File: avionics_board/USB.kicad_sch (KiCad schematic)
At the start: 3 parts, among them J11 10155435-00011LF

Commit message: checking AUX and SCI, tweak BOM
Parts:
- J11: MANUFACTURER (none) -> Amphenol; Manufacturer Amphenol -> (none); PARTREV (none) -> 10155435-00011LF; Part Number 10155435-00011LF -> (none)
- R43, R44: MANUFACTURER (none) -> YAGEO; Manufacturer YAGEO -> (none); PARTREV (none) -> RC0402FR-075K1L; Part Number RC0402FR-075K1L -> (none)
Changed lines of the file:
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@@
-			)
-		)
-		(property "Manufacturer" "YAGEO"
-			(at 175.895 94.615 0)
-			(effects
-				(font
-					(size 1.27 1.27)
-				)
-				(hide yes)
-			)
-		)
-		(property "Part Number" "RC0402FR-075K1L"
-			(at 175.895 94.615 0)
-			(effects
-				(font
-					(size 1.27 1.27)
-				)
-				(hide yes)
 			)
 		)
@@
 			)
 		)
-		(property "MANUFACTURER" ""
+		(property "MANUFACTURER" "YAGEO"
 			(at 175.895 94.615 0)
 			(effects
@@
 			)
 		)
-		(property "PARTREV" ""
+		(property "PARTREV" "RC0402FR-075K1L"
 			(at 175.895 94.615 0)
 			(effects
@@
 			(project "sci_board"
 				(path "/b4b2c88d-f6cd-4e60-862d-e21f68728580/840799ac-4fe6-4a8e-96a2-299affeec8e4/6b5440ce-79ea-4c41-89e9-7a3077535944"
-					(reference "R16")
+					(reference "R18")
 					(unit 1)
 				)
@@
 			)
 		)
-		(property "Manufacturer" "YAGEO"
-			(at 132.08 81.915 0)
-			(effects
-				(font
-					(size 1.27 1.27)
-				)
-				(hide yes)
-			)
-		)
-		(property "Part Number" "RC0402FR-075K1L"
-			(at 132.08 81.915 0)
-			(effects
-				(font
-					(size 1.27 1.27)
-				)
-				(hide yes)
-			)
-		)
 		(property "Tolerance" "1"
 			(at 132.08 81.915 0)
@@
 			)
 		)
-		(property "MANUFACTURER" ""
+		(property "MANUFACTURER" "YAGEO"
 			(at 132.08 81.915 0)
 			(effects
@@
 			)
 		)
-		(property "PARTREV" ""
+		(property "PARTREV" "RC0402FR-075K1L"
 			(at 132.08 81.915 0)
 			(effects
@@
 			(project "sci_board"
 				(path "/b4b2c88d-f6cd-4e60-862d-e21f68728580/840799ac-4fe6-4a8e-96a2-299affeec8e4/6b5440ce-79ea-4c41-89e9-7a3077535944"
-					(reference "R15")
+					(reference "R17")
 					(unit 1)
 				)
@@
 			)
 		)
-		(property "Description" ""
+		(property "Description" "USB connector"
 			(at 153.67 89.535 0)
 			(effects
@@
 			)
 		)
-		(property "Manufacturer" "Amphenol"
-			(at 153.67 89.535 0)
-			(effects
-				(font
-					(size 1.27 1.27)
-				)
-				(hide yes)
-			)
-		)
-		(property "Part Number" " 10155435-00011LF"
-			(at 153.67 89.535 0)
-			(effects
-				(font
-					(size 1.27 1.27)
-				)
-				(hide yes)
-			)
-		)
-		(property "MANUFACTURER" ""
+		(property "MANUFACTURER" "Amphenol"
 			(at 153.67 89.535 0)
 			(effects
@@
 			)
 		)
-		(property "PARTREV" ""
-			(at 153.67 89.535 0)
-			(effects
+		(property "PARTREV" " 10155435-00011LF"
+			(at 153.67 89.535 0)
+			(effects

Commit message: check BOM and footprints for SCI and AUX
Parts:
- R43, R44: Note (none) -> USB
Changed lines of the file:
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@@
+			)
+		)
+		(property "Note" "USB"
+			(at 175.895 94.615 0)
+			(effects
+				(font
+					(size 1.27 1.27)
+				)
+				(hide yes)
 			)
 		)
@@
 			(at 132.08 81.915 0)
 			(effects
+				(font
+					(size 1.27 1.27)
+				)
+				(hide yes)
+			)
+		)
+		(property "Note" "USB"
+			(at 132.08 81.915 0)
+			(effects

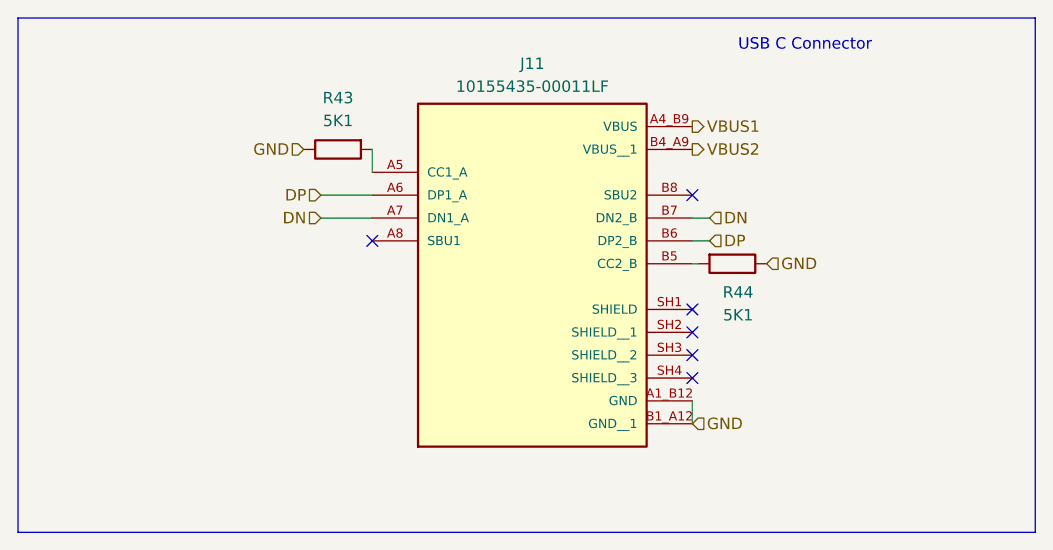
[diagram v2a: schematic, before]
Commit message: full science board with camera switches
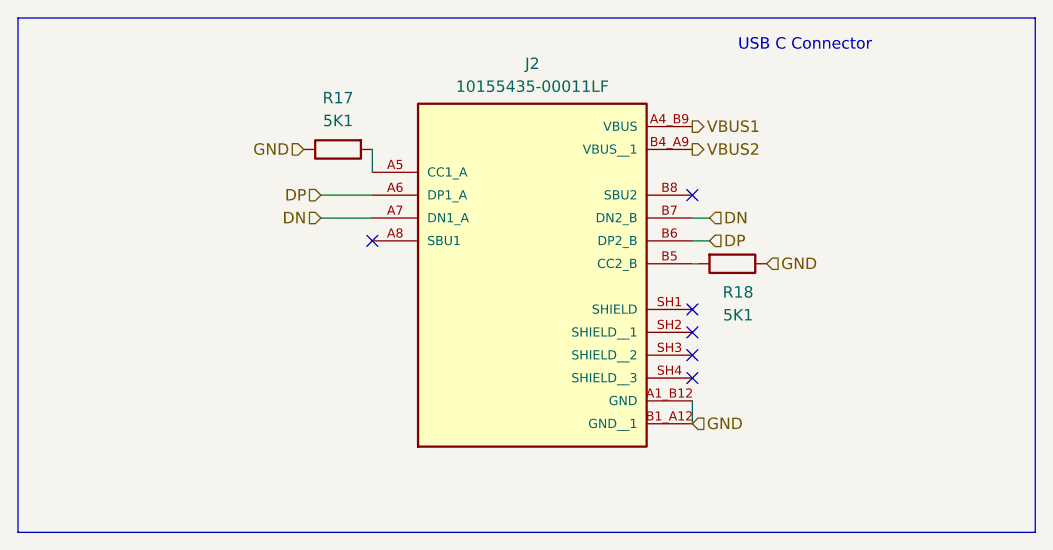
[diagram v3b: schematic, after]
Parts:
- renumbered J11 to J2, R43 to R17, R44 to R18
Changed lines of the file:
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@@
 (kicad_sch
-	(version 20231120)
+	(version 20250114)
 	(generator "eeschema")
-	(generator_version "8.0")
+	(generator_version "9.0")
 	(paper "A4")
-	(no_connect
-		(at 171.45 86.995)
-	)
-	(no_connect
-		(at 171.45 102.235)
-	)
-	(no_connect
-		(at 171.45 107.315)
-	)
-	(no_connect
-		(at 171.45 99.695)
-	)
-	(no_connect
-		(at 135.89 92.075)
-	)
-	(no_connect
-		(at 171.45 104.775)
-	)
-	(wire
-		(pts
-			(xy 173.355 92.075) (xy 171.45 92.075)
-		)
-		(stroke
-			(width 0)
-			(type default)
-		)
-	)
-	(wire
-		(pts
-			(xy 173.355 89.535) (xy 171.45 89.535)
-		)
-		(stroke
-			(width 0)
-			(type default)
-		)
-	)
-	(wire
-		(pts
-			(xy 130.175 89.535) (xy 135.89 89.535)
-		)
-		(stroke
-			(width 0)
-			(type default)
-		)
-	)
-	(wire
-		(pts
-			(xy 130.175 86.995) (xy 135.89 86.995)
-		)
-		(stroke
-			(width 0)
-			(type default)
-		)
-	)
-	(wire
-		(pts
-			(xy 135.89 81.915) (xy 135.89 84.455)
-		)
-		(stroke
-			(width 0)
-			(type default)
-		)
-	)
-	(wire
-		(pts
-			(xy 171.45 109.855) (xy 171.45 112.395)
-		)
-		(stroke
-			(width 0)
-			(type default)
-		)
-	)
-	(wire
-		(pts
-			(xy 172.085 94.615) (xy 171.45 94.615)
-		)
-		(stroke
-			(width 0)
-			(type default)
-		)
-	)
 	(rectangle
 		(start 96.52 67.31)
@@
 		)
 	)
+	(no_connect
+		(at 171.45 86.995)
+	)
+	(no_connect
+		(at 171.45 102.235)
+	)
+	(no_connect
+		(at 171.45 107.315)
+	)
+	(no_connect
+		(at 171.45 99.695)
+	)
+	(no_connect
+		(at 135.89 92.075)
+	)
+	(no_connect
+		(at 171.45 104.775)
+	)
+	(wire
+		(pts
+			(xy 173.355 92.075) (xy 171.45 92.075)
+		)
+		(stroke
+			(width 0)
+			(type default)
+		)
+	)
+	(wire
+		(pts
+			(xy 173.355 89.535) (xy 171.45 89.535)
+		)
+		(stroke
+			(width 0)
+			(type default)
+		)
+	)
+	(wire
+		(pts
+			(xy 130.175 89.535) (xy 135.89 89.535)
+		)
+		(stroke
+			(width 0)
+			(type default)
+		)
+	)
+	(wire
+		(pts
+			(xy 130.175 86.995) (xy 135.89 86.995)
+		)
+		(stroke
+			(width 0)
+			(type default)
+		)
+	)
+	(wire
+		(pts
+			(xy 135.89 81.915) (xy 135.89 84.455)
+		)
+		(stroke
+			(width 0)
+			(type default)
+		)
+	)
+	(wire
+		(pts
+			(xy 171.45 109.855) (xy 171.45 112.395)
+		)
+		(stroke
+			(width 0)
+			(type default)
+		)
+	)
+	(wire
+		(pts
+			(xy 172.085 94.615) (xy 171.45 94.615)
+		)
+		(stroke
+			(width 0)
+			(type default)
+		)
+	)
 	(hierarchical_label "DN"
 		(shape input)
 		(at 173.355 89.535 0)
-		(fields_autoplaced yes)
 		(effects
 			(font
@@
 		(shape input)
 		(at 173.355 92.075 0)
-		(fields_autoplaced yes)
 		(effects
 			(font
@@
 		(shape output)
 		(at 171.45 79.375 0)
-		(fields_autoplaced yes)
 		(effects
 			(font
@@
 		(shape input)
 		(at 130.175 89.535 180)
-		(fields_autoplaced yes)
 		(effects
 			(font
@@
 		(shape input)
 		(at 128.27 81.915 180)
-		(fields_autoplaced yes)
 		(effects
 			(font
@@
 		(shape input)
 		(at 171.45 112.395 0)
-		(fields_autoplaced yes)
 		(effects
 			(font
@@
 		(shape output)
 		(at 171.45 81.915 0)
-		(fields_autoplaced yes)
 		(effects
 			(font
@@
 		(shape input)
 		(at 179.705 94.615 0)
-		(fields_autoplaced yes)
 		(effects
 			(font
@@
 		(shape input)
 		(at 130.175 86.995 180)
-		(fields_autoplaced yes)
 		(effects
 			(font
@@
 		(on_board yes)
 		(dnp no)
-		(property "Reference" "R44"
+		(property "Reference" "R18"
 			(at 176.53 97.79 90)
 			(effects
@@
 		(on_board yes)
 		(dnp no)
-		(property "Reference" "R43"
+		(property "Reference" "R17"
 			(at 132.08 76.2 90)
 			(effects
@@
 		(dnp no)
 		(fields_autoplaced yes)
-		(property "Reference" "J11"
+		(property "Reference" "J2"
 			(at 153.67 72.39 0)
 			(effects

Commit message: cleanup and bom
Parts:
- renumbered R17 to R11, R18 to R12
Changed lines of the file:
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@@
 		(on_board yes)
 		(dnp no)
-		(property "Reference" "R18"
+		(property "Reference" "R12"
 			(at 176.53 97.79 90)
 			(effects
@@
 			(project "sci_board"
 				(path "/b4b2c88d-f6cd-4e60-862d-e21f68728580/840799ac-4fe6-4a8e-96a2-299affeec8e4/6b5440ce-79ea-4c41-89e9-7a3077535944"
-					(reference "R18")
+					(reference "R12")
 					(unit 1)
 				)
@@
 		(on_board yes)
 		(dnp no)
-		(property "Reference" "R17"
+		(property "Reference" "R11"
 			(at 132.08 76.2 90)
 			(effects
@@
 			(project "sci_board"
 				(path "/b4b2c88d-f6cd-4e60-862d-e21f68728580/840799ac-4fe6-4a8e-96a2-299affeec8e4/6b5440ce-79ea-4c41-89e9-7a3077535944"
-					(reference "R17")
-					(unit 1)
-				)
+					(reference "R11")
+					(unit 1)
+				)

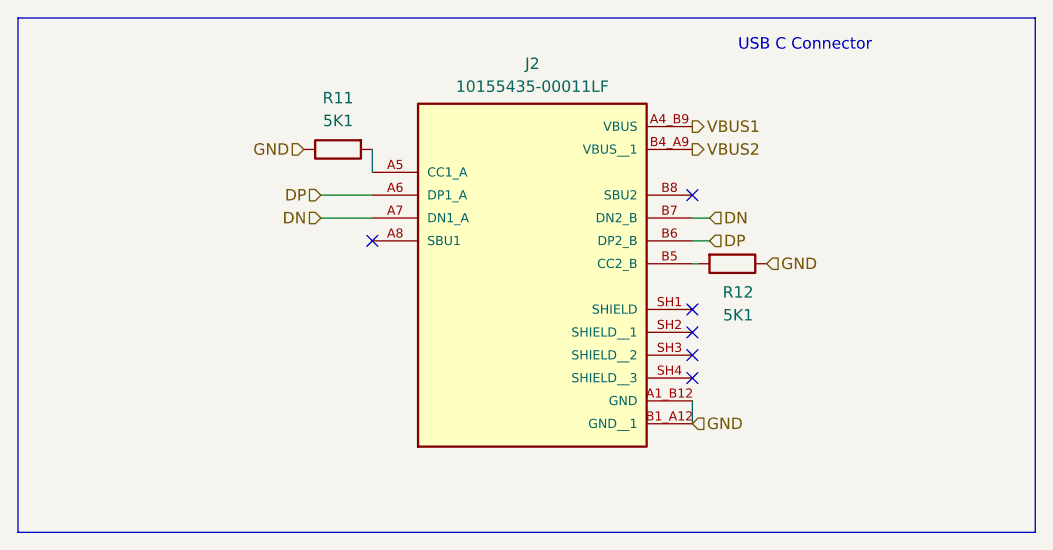
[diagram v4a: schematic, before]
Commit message: AVI board simplified and cleaned up
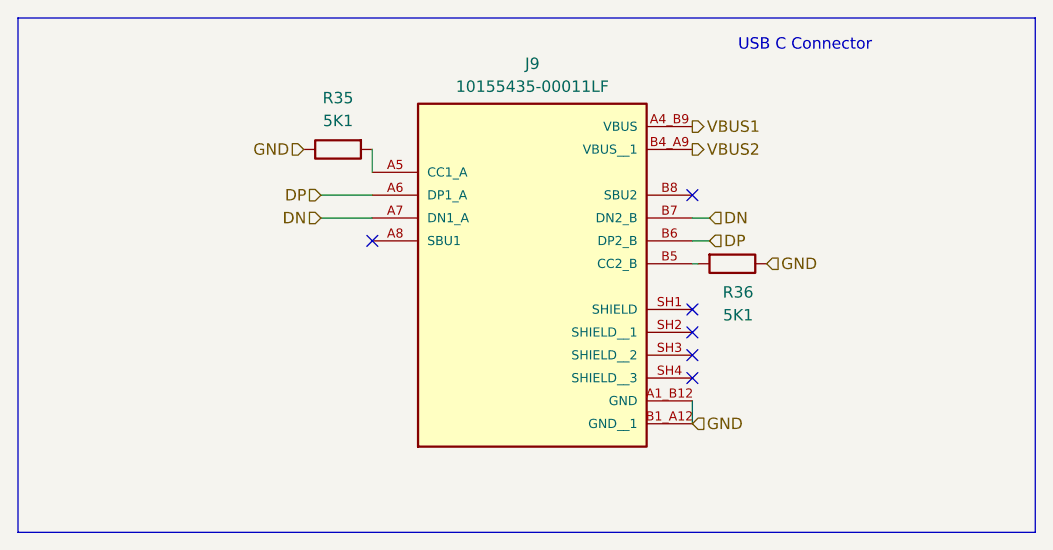
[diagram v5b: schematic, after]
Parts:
- renumbered J2 to J9, R11 to R35, R12 to R36
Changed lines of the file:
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@@
 		(on_board yes)
 		(dnp no)
-		(property "Reference" "R12"
+		(property "Reference" "R36"
 			(at 176.53 97.79 90)
 			(effects
@@
 			(project "AVIONICS_BOARD"
 				(path "/f6cc00ab-17f1-4973-862f-7ac95fe70668/00000000-0000-0000-0000-00005ea31c93/8a47ccc3-f8e0-403c-b9fa-fe30da676570"
-					(reference "R43")
+					(reference "R36")
 					(unit 1)
 				)
@@
 		(on_board yes)
 		(dnp no)
-		(property "Reference" "R11"
+		(property "Reference" "R35"
 			(at 132.08 76.2 90)
 			(effects
@@
 			(project "AVIONICS_BOARD"
 				(path "/f6cc00ab-17f1-4973-862f-7ac95fe70668/00000000-0000-0000-0000-00005ea31c93/8a47ccc3-f8e0-403c-b9fa-fe30da676570"
-					(reference "R42")
+					(reference "R35")
 					(unit 1)
 				)
@@
 		(dnp no)
 		(fields_autoplaced yes)
-		(property "Reference" "J2"
+		(property "Reference" "J9"
 			(at 153.67 72.39 0)
 			(effects

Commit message: via - pad distance rules for SCI and AVI
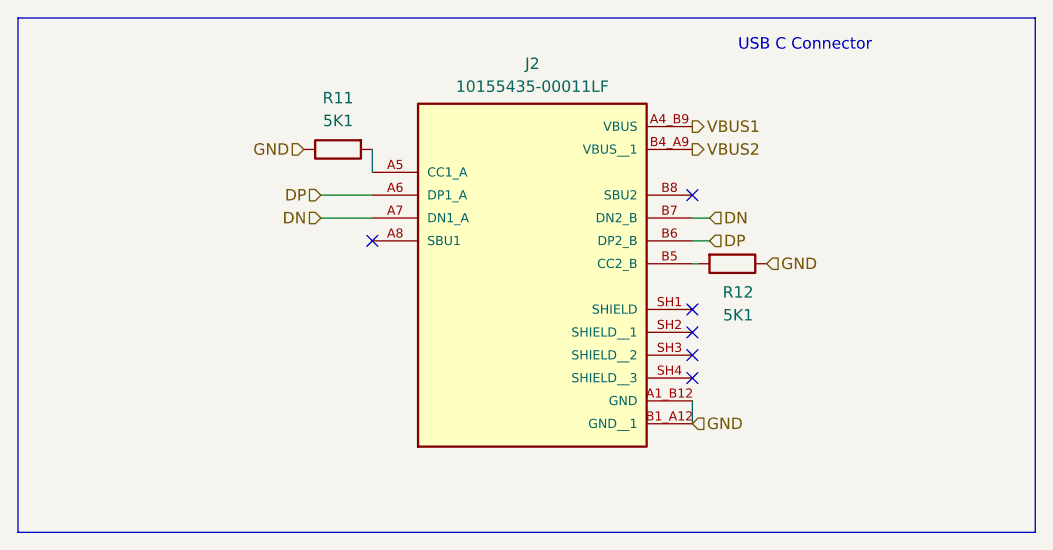
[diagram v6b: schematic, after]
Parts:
- renumbered J9 to J2, R35 to R11, R36 to R12
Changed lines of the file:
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@@
 		(on_board yes)
 		(dnp no)
-		(property "Reference" "R36"
+		(property "Reference" "R12"
 			(at 176.53 97.79 90)
 			(effects
@@
 		(on_board yes)
 		(dnp no)
-		(property "Reference" "R35"
+		(property "Reference" "R11"
 			(at 132.08 76.2 90)
 			(effects
@@
 		(dnp no)
 		(fields_autoplaced yes)
-		(property "Reference" "J9"
+		(property "Reference" "J2"
 			(at 153.67 72.39 0)
 			(effects

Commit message: EPS and AVI joint cleanup
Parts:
- renumbered J2 to J9, R11 to R32, R12 to R33
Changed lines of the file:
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@@
 		(on_board yes)
 		(dnp no)
-		(property "Reference" "R12"
+		(property "Reference" "R33"
 			(at 176.53 97.79 90)
 			(effects
@@
 			(project "AVIONICS_BOARD"
 				(path "/f6cc00ab-17f1-4973-862f-7ac95fe70668/00000000-0000-0000-0000-00005ea31c93/8a47ccc3-f8e0-403c-b9fa-fe30da676570"
-					(reference "R36")
+					(reference "R33")
 					(unit 1)
 				)
@@
 		(on_board yes)
 		(dnp no)
-		(property "Reference" "R11"
+		(property "Reference" "R32"
 			(at 132.08 76.2 90)
 			(effects
@@
 			(project "AVIONICS_BOARD"
 				(path "/f6cc00ab-17f1-4973-862f-7ac95fe70668/00000000-0000-0000-0000-00005ea31c93/8a47ccc3-f8e0-403c-b9fa-fe30da676570"
-					(reference "R35")
+					(reference "R32")
 					(unit 1)
 				)
@@
 		(dnp no)
 		(fields_autoplaced yes)
-		(property "Reference" "J2"
+		(property "Reference" "J9"
 			(at 153.67 72.39 0)
 			(effects

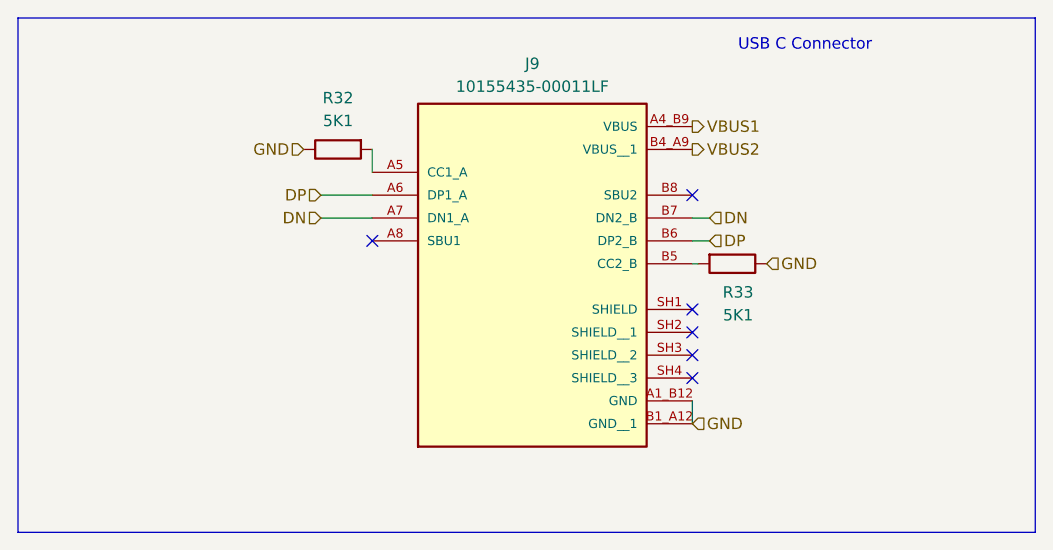
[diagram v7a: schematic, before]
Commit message: SCI AVI and EPS are consistent again
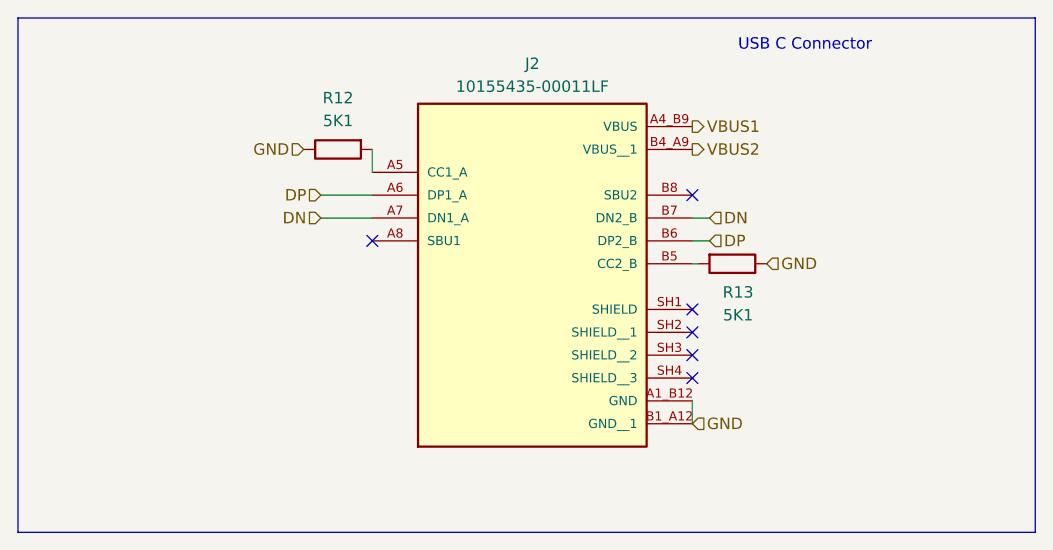
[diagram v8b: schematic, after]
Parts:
- renumbered J9 to J2, R32 to R12, R33 to R13
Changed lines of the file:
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@@
 		(on_board yes)
 		(dnp no)
-		(property "Reference" "R33"
+		(property "Reference" "R13"
 			(at 176.53 97.79 90)
 			(effects
@@
 			(project "sci_board"
 				(path "/b4b2c88d-f6cd-4e60-862d-e21f68728580/840799ac-4fe6-4a8e-96a2-299affeec8e4/6b5440ce-79ea-4c41-89e9-7a3077535944"
-					(reference "R12")
+					(reference "R13")
 					(unit 1)
 				)
@@
 		(on_board yes)
 		(dnp no)
-		(property "Reference" "R32"
+		(property "Reference" "R12"
 			(at 132.08 76.2 90)
 			(effects
@@
 			(project "sci_board"
 				(path "/b4b2c88d-f6cd-4e60-862d-e21f68728580/840799ac-4fe6-4a8e-96a2-299affeec8e4/6b5440ce-79ea-4c41-89e9-7a3077535944"
-					(reference "R11")
+					(reference "R12")
 					(unit 1)
 				)
@@
 		(dnp no)
 		(fields_autoplaced yes)
-		(property "Reference" "J9"
+		(property "Reference" "J2"
 			(at 153.67 72.39 0)
 			(effects
